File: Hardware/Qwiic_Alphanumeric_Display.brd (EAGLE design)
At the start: 40.6 x 27.9 mm, 44 parts, among them J4 Vertical Qwiic Connector, J5 Vertical Qwiic Connector, U2 XC9140

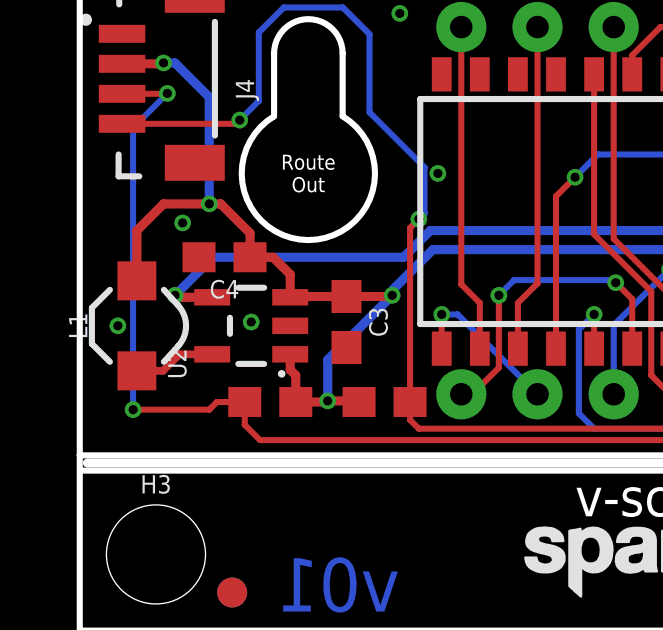
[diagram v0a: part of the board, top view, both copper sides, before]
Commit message: Added test point to 5V rail
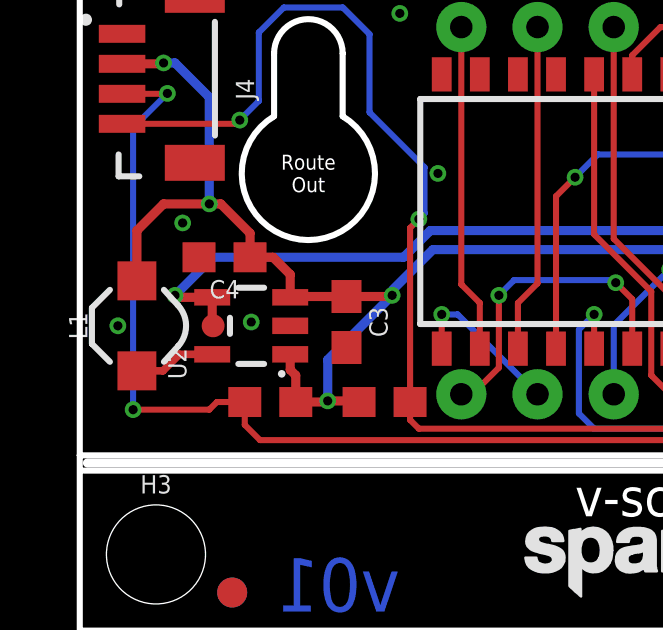
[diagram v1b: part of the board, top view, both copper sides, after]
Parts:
- added 5V: TEST-POINT3, SparkFun-Connectors:PAD.03X.03
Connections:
- net 5V: now also 5V.1
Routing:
- net 5V: track 28.3 -> 29.2 mm
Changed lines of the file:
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@@
 <?xml version="1.0" encoding="utf-8"?>
 <!DOCTYPE eagle SYSTEM "eagle.dtd">
-<eagle version="9.6.2">
+<eagle version="9.5.2">
 <drawing>
 <settings>
@@
 <layer number="42" name="bRestrict" color="1" fill="10" visible="no" active="yes"/>
 <layer number="43" name="vRestrict" color="2" fill="10" visible="no" active="yes"/>
-<layer number="44" name="Drills" color="7" fill="1" visible="yes" active="yes"/>
+<layer number="44" name="Drills" color="7" fill="1" visible="no" active="yes"/>
 <layer number="45" name="Holes" color="7" fill="1" visible="yes" active="yes"/>
-<layer number="46" name="Milling" color="3" fill="1" visible="yes" active="yes"/>
-<layer number="47" name="Measures" color="7" fill="1" visible="yes" active="yes"/>
-<layer number="48" name="Document" color="7" fill="1" visible="yes" active="yes"/>
-<layer number="49" name="Reference" color="7" fill="1" visible="yes" active="yes"/>
-<layer number="50" name="dxf" color="7" fill="1" visible="yes" active="yes"/>
+<layer number="46" name="Milling" color="3" fill="1" visible="no" active="yes"/>
+<layer number="47" name="Measures" color="7" fill="1" visible="no" active="yes"/>
+<layer number="48" name="Document" color="7" fill="1" visible="no" active="yes"/>
+<layer number="49" name="Reference" color="7" fill="1" visible="no" active="yes"/>
+<layer number="50" name="dxf" color="7" fill="1" visible="no" active="yes"/>
 <layer number="51" name="tDocu" color="6" fill="1" visible="yes" active="yes"/>
-<layer number="52" name="bDocu" color="7" fill="1" visible="yes" active="yes"/>
+<layer number="52" name="bDocu" color="7" fill="1" visible="no" active="yes"/>
 <layer number="91" name="Nets" color="2" fill="1" visible="no" active="no"/>
 <layer number="92" name="Busses" color="1" fill="1" visible="no" active="no"/>
@@
 <element name="U$16" library="output" package="30" value="" x="29.718" y="12.7" smashed="yes"/>
 <element name="U$17" library="output" package="G0" value="" x="29.718" y="10.16" smashed="yes"/>
+<element name="5V" library="SparkFun-Connectors" package="PAD.03X.03" value="TEST-POINT3" x="4.445" y="10.16" smashed="yes"/>
 </elements>
 <signals>
@@
 <wire x1="11.684" y1="13.335" x2="21.717" y2="13.335" width="0.3048" layer="16"/>
 <wire x1="21.717" y1="13.335" x2="22.7711" y2="12.2809" width="0.3048" layer="16"/>
+<contactref element="5V" pad="1"/>
+<wire x1="4.445" y1="10.16" x2="4.4149" y2="10.1901" width="0.254" layer="1"/>
+<wire x1="4.4149" y1="10.1901" x2="4.4149" y2="11.11" width="0.3048" layer="1"/>
 </signal>
 </signals>

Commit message: Remove the 5V test point after all!
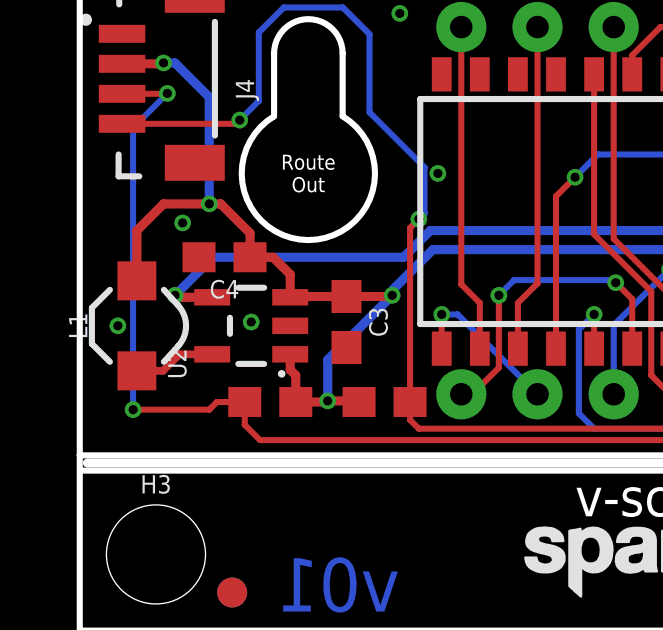
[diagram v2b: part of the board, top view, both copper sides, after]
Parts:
- removed 5V: TEST-POINT3, SparkFun-Connectors:PAD.03X.03
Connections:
- net 5V: no longer 5V.1
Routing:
- net 5V: track 29.2 -> 28.3 mm
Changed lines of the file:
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@@
 <element name="U$16" library="output" package="30" value="" x="29.718" y="12.7" smashed="yes"/>
 <element name="U$17" library="output" package="G0" value="" x="29.718" y="10.16" smashed="yes"/>
-<element name="5V" library="SparkFun-Connectors" package="PAD.03X.03" value="TEST-POINT3" x="4.445" y="10.16" smashed="yes"/>
 </elements>
 <signals>
@@
 <wire x1="11.684" y1="13.335" x2="21.717" y2="13.335" width="0.3048" layer="16"/>
 <wire x1="21.717" y1="13.335" x2="22.7711" y2="12.2809" width="0.3048" layer="16"/>
-<contactref element="5V" pad="1"/>
-<wire x1="4.445" y1="10.16" x2="4.4149" y2="10.1901" width="0.254" layer="1"/>
-<wire x1="4.4149" y1="10.1901" x2="4.4149" y2="11.11" width="0.3048" layer="1"/>
 </signal>
 </signals>

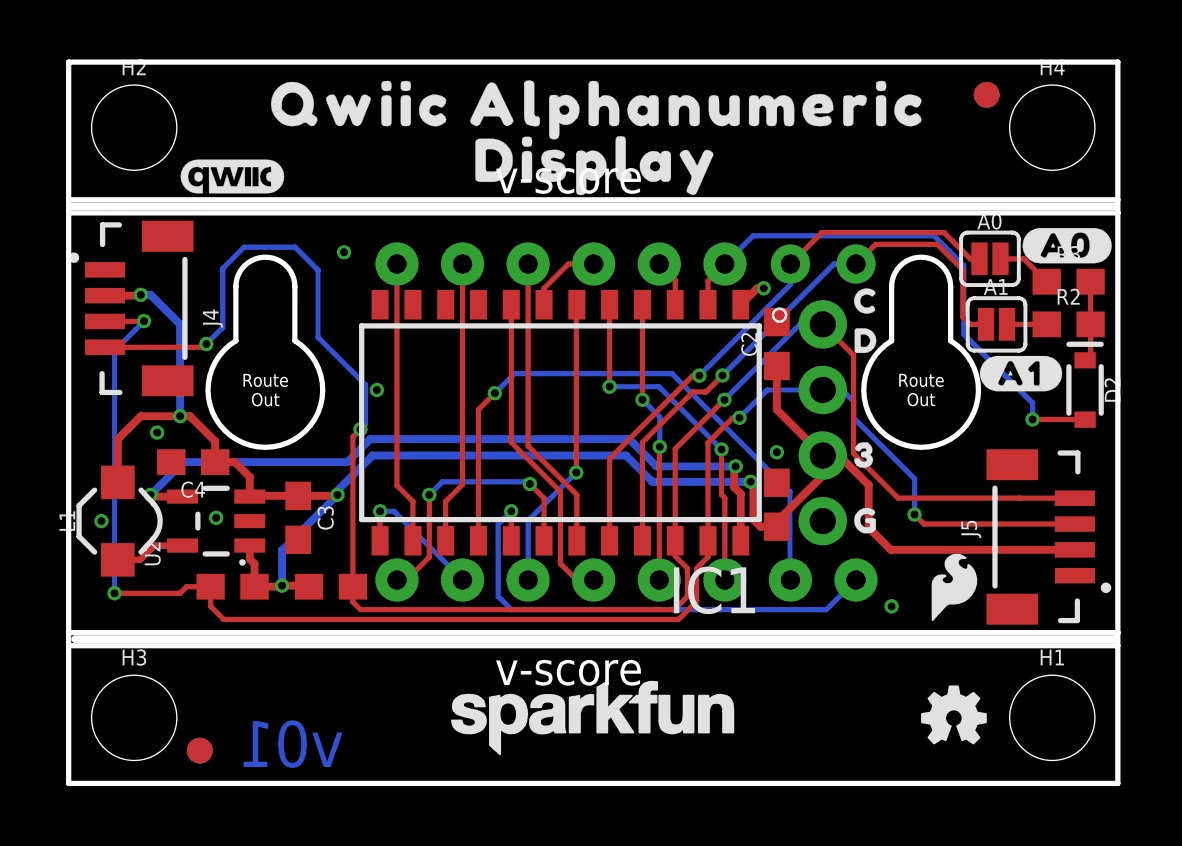
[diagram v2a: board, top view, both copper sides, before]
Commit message: Pete's design updates
* Update address table with "open" and "closed"
* Move address resistors and jumpers
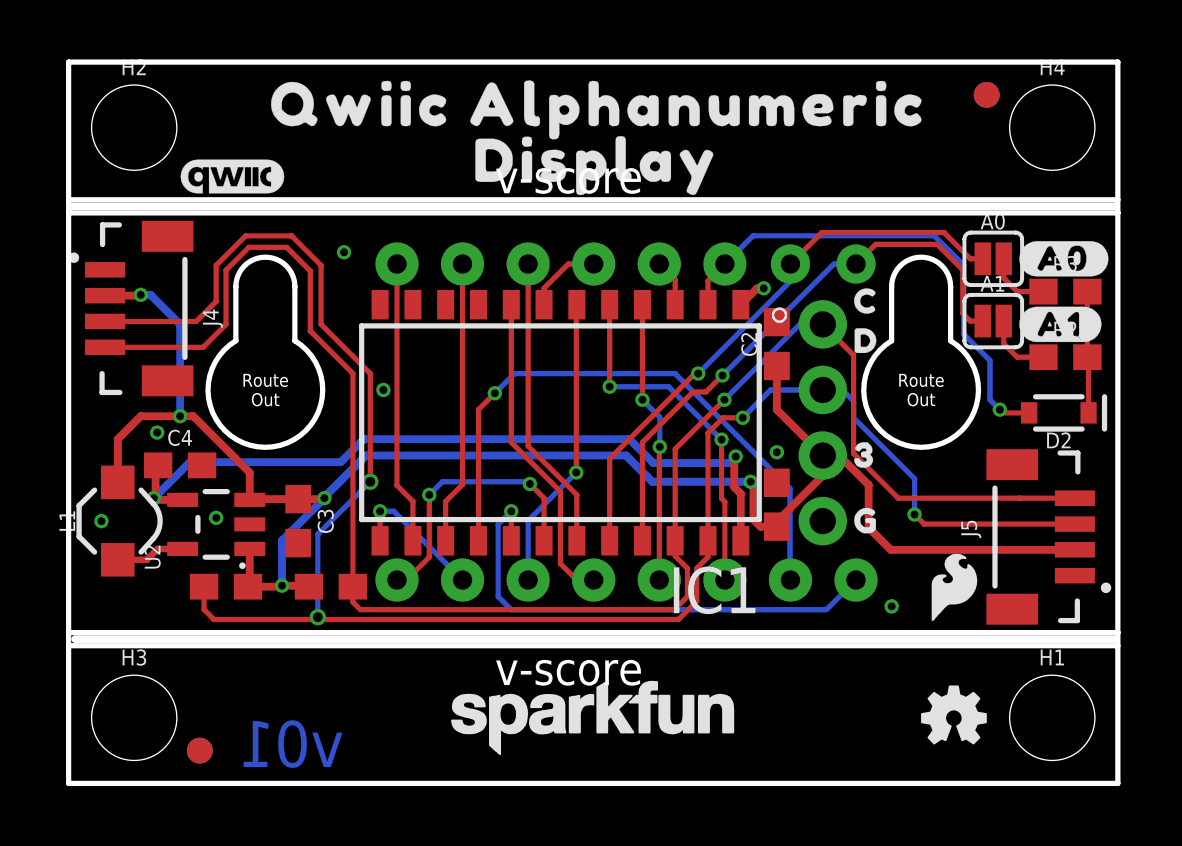
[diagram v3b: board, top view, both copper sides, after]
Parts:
- moved U$13 2.44 mm to (36.8, 17.8)
- moved D2 1.35 mm to (38.4, 14.4), turned to 180 degrees
- moved R2 1.28 mm to (38.6, 16.5)
- moved C4 0.52 mm to (4.32, 12.3), turned to 0 degrees
- moved U$12 0.52 mm to (36.8, 20.3)
- moved R3 0.40 mm to (38.6, 19.1)
- moved R4 0.25 mm to (6.10, 7.62)
- moved A1 0.18 mm to (35.8, 17.9)
- moved A0 0.13 mm to (35.8, 20.3)
- moved C3 0.13 mm to (8.89, 10.2)
- moved U2 0.13 mm to (5.71, 10.0)
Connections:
- net 3.3V: no longer C4.1
- net 5V: now also C4.1
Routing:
- net SDA: track 61.2 -> 71.7 mm
- net COM_A: track 21.1 -> 19.4 mm
- net N$6: track 3.13 -> 4.74 mm
- net 5V: track 28.3 -> 29.9 mm
- net N$2: track 1.54 -> 2.63 mm
- net SCL: track 67.1 -> 66.4 mm, vias 3 -> 1
- net 3.3V: track 67.6 -> 67.1 mm

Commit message: Pete's updates
* Some silk updates: default address and address jumper labels
* Bump version number v01 --> v10
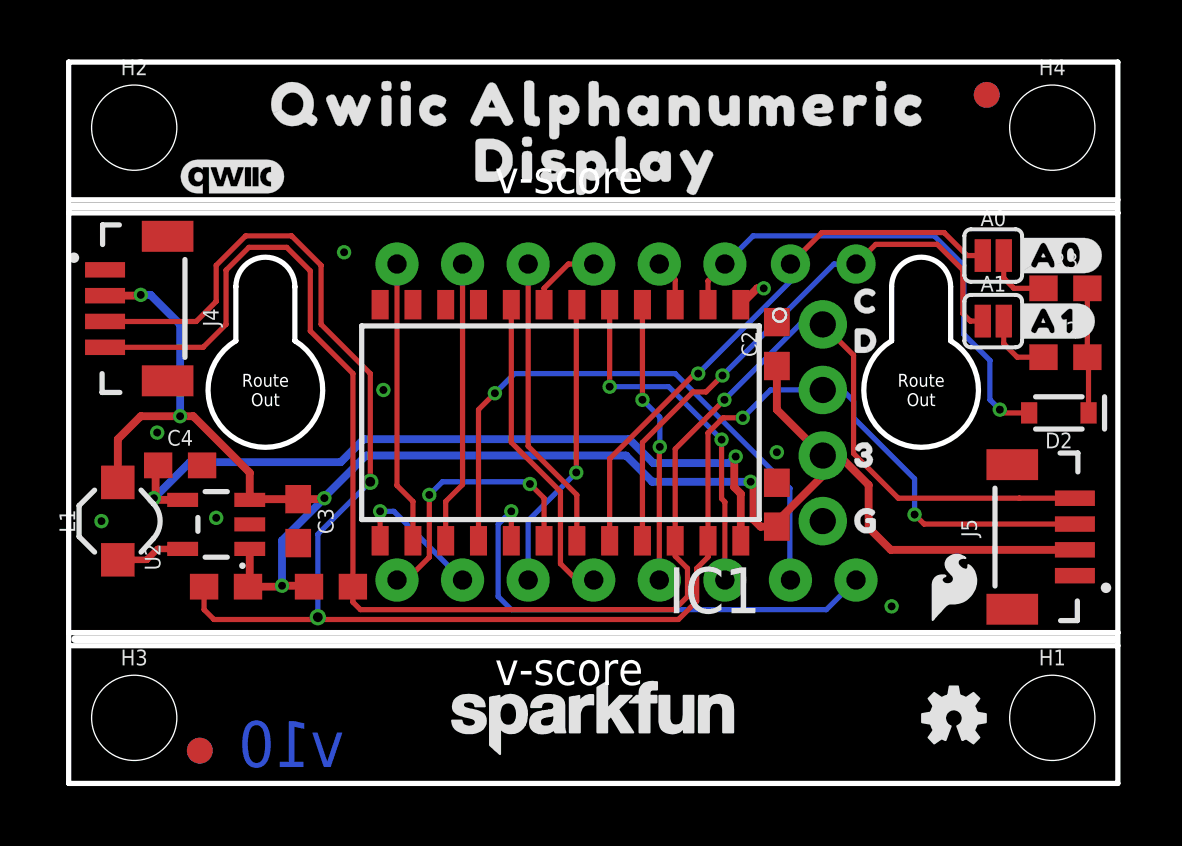
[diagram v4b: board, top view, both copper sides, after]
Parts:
- added U$1: (no value), output:DEFAULT_ADR#_0X700
- moved LOGO2 0.76 mm to (20.3, 1.78)
- moved U$12 0.28 mm to (36.6, 20.4)
- moved U$13 0.28 mm to (36.6, 17.9)
- moved A0 0.13 mm to (35.8, 20.4)
- moved R3 0.13 mm to (38.6, 19.2)
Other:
- board text added: "v10"
- board text removed: "v01"
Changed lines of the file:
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@@
 <?xml version="1.0" encoding="utf-8"?>
 <!DOCTYPE eagle SYSTEM "eagle.dtd">
-<eagle version="9.5.2">
+<eagle version="9.4.2">
 <drawing>
 <settings>
-<setting alwaysvectorfont="no"/>
+<setting alwaysvectorfont="yes"/>
 <setting verticaltext="up"/>
 </settings>
@@
 <text x="16.51" y="3.81" size="1.27" layer="20" font="vector" ratio="15">v-score</text>
 <text x="16.51" y="22.86" size="1.27" layer="20" font="vector" ratio="15">v-score</text>
-<text x="10.668" y="0.635" size="1.778" layer="16" font="vector" ratio="15" rot="MR0">v01</text>
+<text x="10.668" y="0.635" size="1.778" layer="16" font="vector" ratio="15" rot="MR0">v10</text>
 <dimension x1="2.54" y1="2.54" x2="2.54" y2="25.4" x3="-8.89" y3="13.97" textsize="1.778" textratio="15" layer="47" unit="inch"/>
 <dimension x1="0" y1="5.842" x2="0" y2="22.098" x3="-1.27" y3="13.97" textsize="1.778" textratio="15" layer="47" unit="inch"/>
@@
 <attribute name="VALUE" x="35.814" y="16.764" size="0.6096" layer="27" font="vector" ratio="20" align="top-center"/>
 </element>
-<element name="A0" library="SparkFun-Jumpers" package="SMT-JUMPER_2_NO_SILK" package3d_urn="urn:adsk.eagle:package:39279/1" value="JUMPER-SMT_2_NO_SILK" x="35.814" y="20.32" smashed="yes">
-<attribute name="NAME" x="35.814" y="21.463" size="0.6096" layer="25" font="vector" ratio="20" align="bottom-center"/>
-<attribute name="VALUE" x="35.814" y="19.177" size="0.6096" layer="27" font="vector" ratio="20" align="top-center"/>
+<element name="A0" library="SparkFun-Jumpers" package="SMT-JUMPER_2_NO_SILK" package3d_urn="urn:adsk.eagle:package:39279/1" value="JUMPER-SMT_2_NO_SILK" x="35.814" y="20.447" smashed="yes">
+<attribute name="NAME" x="35.814" y="21.59" size="0.6096" layer="25" font="vector" ratio="20" align="bottom-center"/>
+<attribute name="VALUE" x="35.814" y="19.304" size="0.6096" layer="27" font="vector" ratio="20" align="top-center"/>
 </element>
 <element name="R2" library="SparkFun-Resistors" package="0603" value="39k" x="38.608" y="16.51" smashed="yes">
@@
 <attribute name="VALUE" x="38.608" y="15.748" size="0.6096" layer="27" font="vector" ratio="20" align="top-center"/>
 </element>
-<element name="R3" library="SparkFun-Resistors" package="0603" value="39k" x="38.608" y="19.05" smashed="yes">
-<attribute name="NAME" x="38.608" y="19.812" size="0.6096" layer="25" font="vector" ratio="20" align="bottom-center"/>
-<attribute name="PROD_ID" value="RES-12377" x="38.608" y="19.05" size="1.778" layer="27" font="vector" ratio="15" display="off"/>
-<attribute name="VALUE" x="38.608" y="18.288" size="0.6096" layer="27" font="vector" ratio="20" align="top-center"/>
+<element name="R3" library="SparkFun-Resistors" package="0603" value="39k" x="38.608" y="19.177" smashed="yes">
+<attribute name="NAME" x="38.608" y="19.939" size="0.6096" layer="25" font="vector" ratio="20" align="bottom-center"/>
+<attribute name="PROD_ID" value="RES-12377" x="38.608" y="19.177" size="1.778" layer="27" font="vector" ratio="15" display="off"/>
+<attribute name="VALUE" x="38.608" y="18.415" size="0.6096" layer="27" font="vector" ratio="20" align="top-center"/>
 </element>
 <element name="D2" library="SparkFun-DiscreteSemi" package="SOD-323" value="250mA/100V" x="38.354" y="14.351" smashed="yes" rot="R180">
@@
 <attribute name="VALUE" x="3.683" y="10.16" size="0.6096" layer="27" font="vector" ratio="20" rot="R90" align="top-center"/>
 </element>
-<element name="LOGO2" library="SparkFun-Aesthetics" package="SFE_LOGO_NAME_.1" value="SFE_LOGO_NAME.1_INCH" x="20.32" y="2.54" smashed="yes" rot="MR0"/>
+<element name="LOGO2" library="SparkFun-Aesthetics" package="SFE_LOGO_NAME_.1" value="SFE_LOGO_NAME.1_INCH" x="20.32" y="1.778" smashed="yes" rot="MR0"/>
 <element name="LOGO3" library="SparkFun-Aesthetics" package="SFE_LOGO_NAME_.1" value="SFE_LOGO_NAME.1_INCH" x="20.32" y="2.54" smashed="yes"/>
 <element name="LOGO4" library="SparkFun-Aesthetics" package="SFE_LOGO_FLAME_.1" value="SFE_LOGO_FLAME.1_INCH" x="34.29" y="7.62" smashed="yes"/>
@@
 <element name="U$10" library="output" package="DISPLAY0" value="" x="14.478" y="24.13" smashed="yes"/>
 <element name="U$11" library="output" package="DISPLAY0" value="" x="26.162" y="24.13" smashed="yes" rot="MR0"/>
-<element name="U$12" library="output" package="#A0#0" value="" x="36.83" y="20.32" smashed="yes"/>
-<element name="U$13" library="output" package="#A1#0" value="" x="36.83" y="17.78" smashed="yes"/>
+<element name="U$12" library="output" package="#A0#0" value="" x="36.576" y="20.447" smashed="yes"/>
+<element name="U$13" library="output" package="#A1#0" value="" x="36.576" y="17.907" smashed="yes"/>
 <element name="U$14" library="output" package="C0" value="" x="29.718" y="18.669" smashed="yes"/>
 <element name="U$15" library="output" package="D0" value="" x="29.718" y="17.145" smashed="yes"/>
 <element name="U$16" library="output" package="30" value="" x="29.718" y="12.7" smashed="yes"/>
 <element name="U$17" library="output" package="G0" value="" x="29.718" y="10.16" smashed="yes"/>
+<element name="U$1" library="output" package="DEFAULT_ADR#_0X700" value="" x="27.813" y="4.191" smashed="yes" rot="MR0"/>
 </elements>
 <signals>
@@
 <contactref element="IC1" pad="20"/>
 <wire x1="27.958" y1="20.118" x2="29.176" y2="21.336" width="0.2032" layer="1"/>
-<wire x1="33.909" y1="21.336" x2="34.925" y2="20.32" width="0.2032" layer="1"/>
-<wire x1="34.925" y1="20.32" x2="35.4076" y2="20.32" width="0.2032" layer="1"/>
+<wire x1="33.909" y1="21.336" x2="34.798" y2="20.447" width="0.2032" layer="1"/>
+<wire x1="34.798" y1="20.447" x2="35.4076" y2="20.447" width="0.2032" layer="1"/>
 <wire x1="29.176" y1="21.336" x2="33.909" y2="21.336" width="0.2032" layer="1"/>
 <wire x1="20.955" y1="9.398" x2="20.955" y2="12.573" width="0.2032" layer="1"/>
@@
 <contactref element="A0" pad="2"/>
 <contactref element="R3" pad="1"/>
-<wire x1="36.742" y1="19.05" x2="37.758" y2="19.05" width="0.2032" layer="1"/>
-<wire x1="36.2204" y1="20.32" x2="36.2204" y2="19.5716" width="0.2032" layer="1"/>
-<wire x1="36.742" y1="19.05" x2="36.2204" y2="19.5716" width="0.2032" layer="1"/>
+<wire x1="36.615" y1="19.177" x2="37.758" y2="19.177" width="0.2032" layer="1"/>
+<wire x1="36.2204" y1="20.447" x2="36.2204" y2="19.5716" width="0.2032" layer="1"/>
+<wire x1="36.615" y1="19.177" x2="36.2204" y2="19.5716" width="0.2032" layer="1"/>
 </signal>
 <signal name="N$6">
@@
 <contactref element="R3" pad="2"/>
 <contactref element="D2" pad="C"/>
-<wire x1="39.458" y1="19.05" x2="39.458" y2="16.51" width="0.2032" layer="1"/>
+<wire x1="39.458" y1="19.177" x2="39.458" y2="16.51" width="0.2032" layer="1"/>
 <wire x1="39.504" y1="14.351" x2="39.504" y2="16.51" width="0.2032" layer="1"/>
 <wire x1="39.458" y1="16.51" x2="39.504" y2="16.51" width="0.2032" layer="1"/>
